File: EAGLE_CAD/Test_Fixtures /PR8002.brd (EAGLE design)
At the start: 118.5 x 99.3 mm, 61 parts, among them J1 M3_SCREW_POST

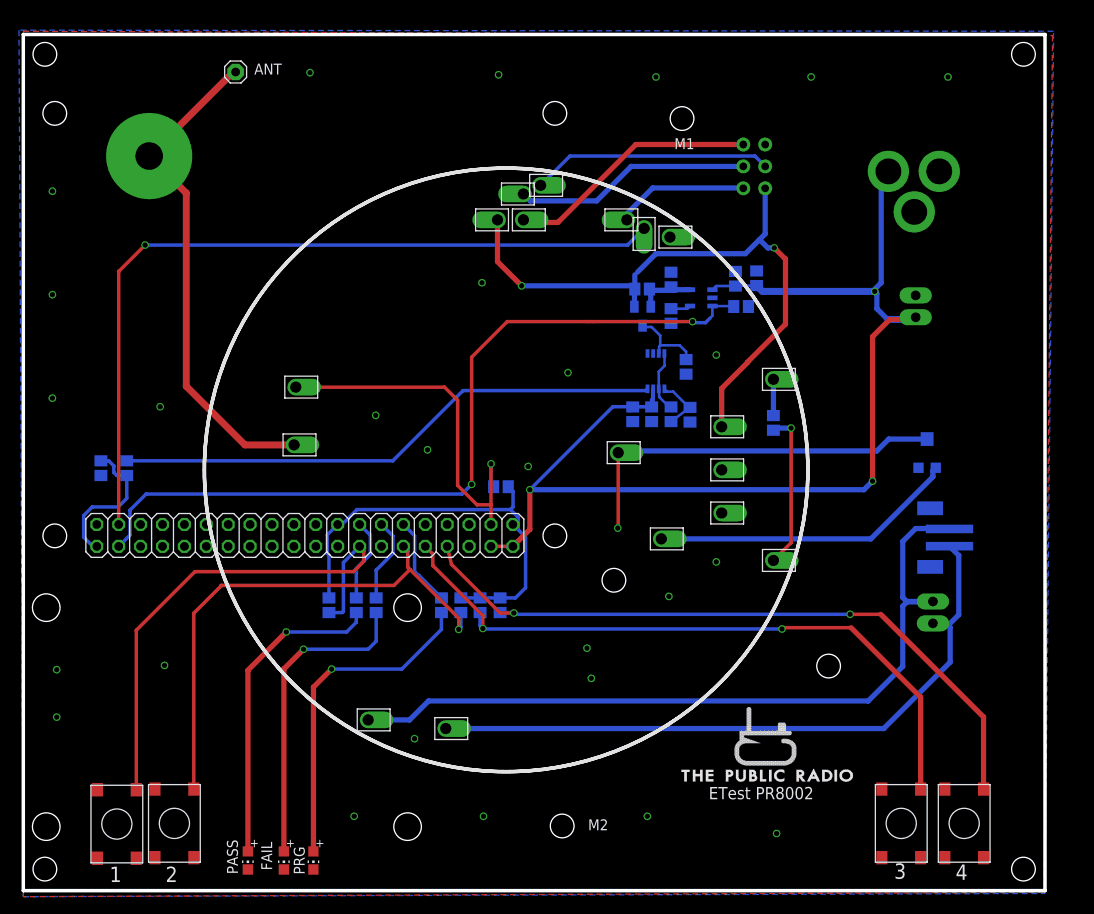
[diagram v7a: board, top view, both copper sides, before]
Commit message: edited test board outline
also aligned corner holes to a grid & moved ISP slightly
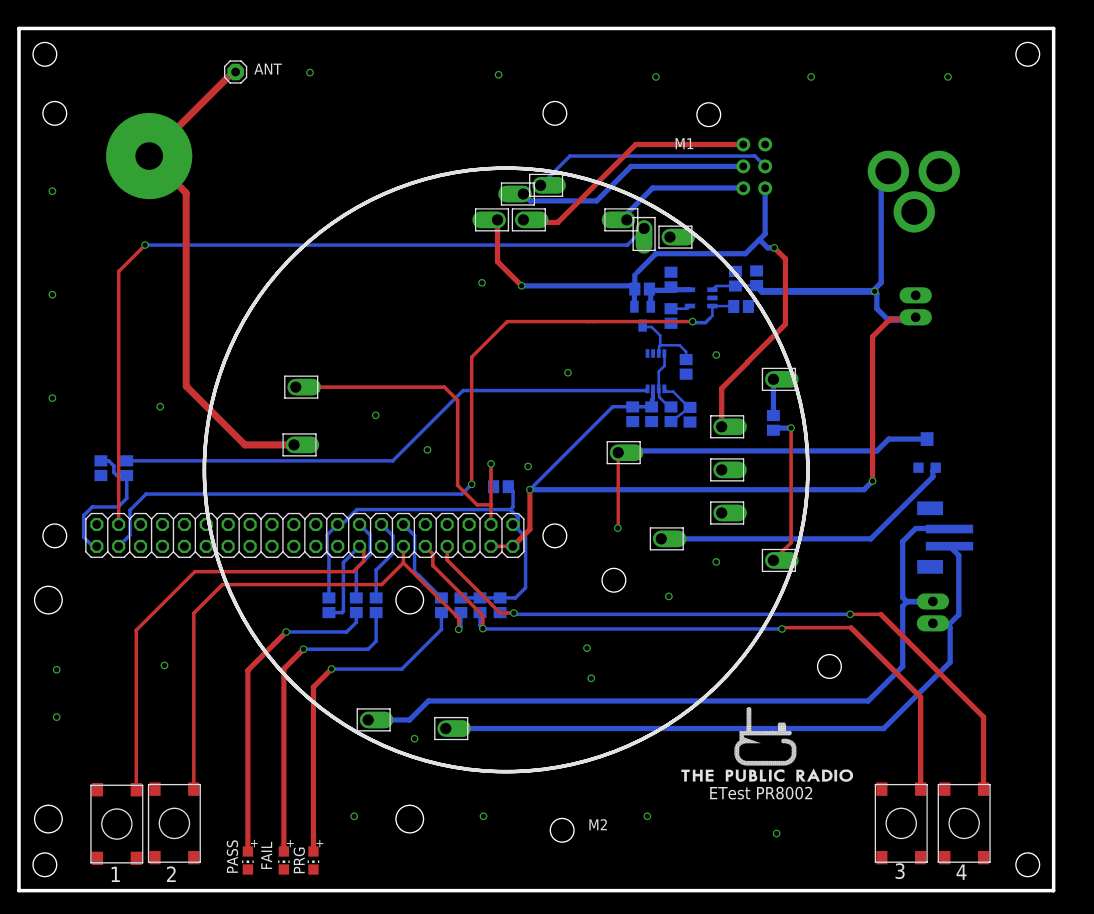
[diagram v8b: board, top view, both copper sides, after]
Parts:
- moved U$25 0.91 mm to (25.0, 21.0)
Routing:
- net TAC3: track 62.2 -> 61.6 mm
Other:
- board size 118.5 x 99.3 mm -> 120 x 100 mm
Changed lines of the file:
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@@
 <?xml version="1.0" encoding="utf-8"?>
 <!DOCTYPE eagle SYSTEM "eagle.dtd">
-<eagle version="6.6.0">
+<eagle version="7.2.0">
 <drawing>
 <settings>
@@
 <rectangle x1="56.8949" y1="26.4365" x2="56.9711" y2="26.4619" layer="26" rot="R180"/>
 <rectangle x1="56.9203" y1="26.4619" x2="57.0981" y2="26.4873" layer="26" rot="R180"/>
-<wire x1="0.5" y1="0" x2="119" y2="0" width="0.4064" layer="20"/>
-<wire x1="119" y1="0" x2="119" y2="99.3" width="0.4064" layer="20"/>
-<wire x1="119" y1="99.3" x2="0.5" y2="99.3" width="0.4064" layer="20"/>
-<wire x1="0.5" y1="99.3" x2="0.5" y2="0" width="0.4064" layer="20"/>
+<wire x1="0" y1="0" x2="120" y2="0" width="0.4064" layer="20"/>
+<wire x1="120" y1="0" x2="120" y2="100" width="0.4064" layer="20"/>
+<wire x1="120" y1="100" x2="0" y2="100" width="0.4064" layer="20"/>
+<wire x1="0" y1="100" x2="0" y2="0" width="0.4064" layer="20"/>
 <text x="80" y="10.6" size="1.4224" layer="25" font="vector" ratio="18">ETest PR8002</text>
 <wire x1="3.65" y1="93.65" x2="62.65" y2="93.65" width="0" layer="22"/>
@@
 <text x="22.675" y="68.225" size="1.778" layer="26" font="vector" ratio="16" rot="MR0">RPI B+</text>
 <circle x="56.5" y="48.8" radius="35" width="0.4064" layer="21"/>
-<hole x="63" y="7.5" drill="2.75"/>
-<hole x="76.9" y="89.55" drill="2.75"/>
+<hole x="63" y="7" drill="2.75"/>
+<hole x="80" y="90" drill="2.75"/>
 <text x="76" y="86" size="1.27" layer="21" font="vector" ratio="16">M1</text>
 <text x="66" y="7" size="1.27" layer="21" font="vector" ratio="16">M2</text>
-<hole x="3" y="2.5" drill="2.75"/>
+<hole x="3" y="3" drill="2.75"/>
 <hole x="3" y="97" drill="2.75"/>
-<hole x="116.5" y="97" drill="2.75"/>
+<hole x="117" y="97" drill="2.75"/>
 <hole x="69" y="36" drill="2.75"/>
-<hole x="116.5" y="2.5" drill="2.75"/>
-<hole x="93.9" y="26.05" drill="2.75"/>
+<hole x="117" y="3" drill="2.75"/>
+<hole x="94" y="26" drill="2.75"/>
 <text x="107.5" y="70.5" size="1.27" layer="22" font="vector" ratio="18" rot="MR270">+   -</text>
-<dimension x1="0.5" y1="-0.7" x2="37.75" y2="99.25" x3="126" y3="49.275" textsize="1.27" textratio="18" layer="20" dtype="vertical" unit="inch"/>
-<dimension x1="0.5" y1="99.675" x2="119" y2="99.3" x3="59.75" y3="102.5" textsize="1.27" textratio="18" layer="20" dtype="horizontal" unit="inch"/>
 </plain>
 <attributes>
@@
 <pass name="Default">
 <param name="RoutingGrid" value="50mil"/>
+<param name="AutoGrid" value="1"/>
+<param name="Efforts" value="0"/>
+<param name="TopRouterVariant" value="1"/>
 <param name="tpViaShape" value="round"/>
 <param name="PrefDir.1" value="|"/>
@@
 <attribute name="VALUE" x="23.855" y="91.775" size="1.27" layer="27"/>
 </element>
-<element name="U$25" library="PR_Parts_Library" package="SFUN_POCKETPROGRAMMER" value="SFUN_POCKETPROGRAMMER" x="24.75" y="20.125" rot="MR90"/>
+<element name="U$25" library="PR_Parts_Library" package="SFUN_POCKETPROGRAMMER" value="SFUN_POCKETPROGRAMMER" x="25" y="21" rot="MR90"/>
 <element name="GPIO" library="pinhead" package="2X20" value="" x="33.155" y="41.2" smashed="yes" rot="R180">
 <attribute name="NAME" x="27.555" y="46.025" size="1.27" layer="26" font="vector" ratio="16" rot="MR180"/>
@@
 <contactref element="ISP1" pad="6"/>
 <polygon width="0.6096" layer="1">
-<vertex x="0.5" y="99.675"/>
-<vertex x="119.875" y="99.175"/>
-<vertex x="118.875" y="-0.2"/>
-<vertex x="0.5" y="-0.7"/>
+<vertex x="0" y="100"/>
+<vertex x="120" y="100"/>
+<vertex x="120" y="0"/>
+<vertex x="0" y="0"/>
 </polygon>
 <polygon width="0.4064" layer="16">
-<vertex x="0.5" y="-0.7"/>
-<vertex x="119" y="-0.325"/>
-<vertex x="120" y="99.675"/>
-<vertex x="0" y="99.8"/>
+<vertex x="0" y="0"/>
+<vertex x="120" y="0"/>
+<vertex x="120" y="100"/>
+<vertex x="0" y="100"/>
 </polygon>
 <contactref element="U$3" pad="P$1"/>
@@
 <contactref element="GPIO" pad="8"/>
 <contactref element="R10" pad="2"/>
-<wire x1="49.665" y1="39.93" x2="50.165" y2="37.835" width="0.4064" layer="1"/>
 <via x="57.4" y="32.2" extent="1-16" drill="0.6" diameter="0.6096"/>
 <wire x1="57.4" y1="32.2" x2="57.35" y2="32.25" width="0.4064" layer="16"/>
@@
 <wire x1="96.4" y1="32.05" x2="99.95" y2="32.05" width="0.4064" layer="1"/>
 <wire x1="57.35" y1="32.25" x2="55.8" y2="32.25" width="0.4064" layer="16"/>
-<wire x1="50.165" y1="37.835" x2="55.8" y2="32.2" width="0.4064" layer="1"/>
 <wire x1="55.8" y1="32.2" x2="57.4" y2="32.2" width="0.4064" layer="1"/>
 <wire x1="99.95" y1="32.05" x2="111.875" y2="20.125" width="0.6096" layer="1"/>
 <wire x1="111.875" y1="20.125" x2="111.875" y2="11.775" width="0.6096" layer="1"/>
+<wire x1="55.8" y1="32.2" x2="49.665" y2="38.335" width="0.4064" layer="1"/>
+<wire x1="49.665" y1="38.335" x2="49.665" y2="39.93" width="0.4064" layer="1"/>
 </signal>
 <signal name="TAC2">
@@
 <contactref element="GPIO" pad="12"/>
 <contactref element="R12" pad="2"/>
-<wire x1="44.585" y1="39.93" x2="45.1" y2="39.415" width="0.4064" layer="1"/>
-<wire x1="45.1" y1="39.415" x2="45.1" y2="37.5" width="0.4064" layer="1"/>
-<wire x1="45.1" y1="37.5" x2="45.35" y2="37.25" width="0.4064" layer="1"/>
-<wire x1="45.35" y1="37.25" x2="51" y2="31.6" width="0.4064" layer="1"/>
 <wire x1="51" y1="31.6" x2="51" y2="30.3" width="0.4064" layer="1"/>
 <via x="51" y="30.3" extent="1-16" drill="0.6" diameter="0.6096"/>
 <wire x1="51" y1="30.3" x2="50.9" y2="30.2" width="0.4064" layer="16"/>
-<wire x1="23.4" y1="35.4" x2="23.5" y2="35.4" width="0.4064" layer="1"/>
-<wire x1="23.5" y1="35.4" x2="43.5" y2="35.4" width="0.4064" layer="1"/>
-<wire x1="43.5" y1="35.4" x2="45.35" y2="37.25" width="0.4064" layer="1"/>
 <wire x1="51.25" y1="32.25" x2="51.25" y2="30.55" width="0.4064" layer="16"/>
 <wire x1="51.25" y1="30.55" x2="51" y2="30.3" width="0.4064" layer="16"/>
 <wire x1="20.275" y1="11.775" x2="20.275" y2="32.175" width="0.4064" layer="1"/>
-<wire x1="20.275" y1="32.175" x2="23.5" y2="35.4" width="0.4064" layer="1"/>
+<wire x1="51" y1="31.6" x2="44.585" y2="38.015" width="0.4064" layer="1"/>
+<wire x1="44.585" y1="38.015" x2="44.585" y2="39.93" width="0.4064" layer="1"/>
+<wire x1="20.275" y1="32.175" x2="23.6" y2="35.5" width="0.4064" layer="1"/>
+<wire x1="23.6" y1="35.5" x2="42.07" y2="35.5" width="0.4064" layer="1"/>
+<wire x1="42.07" y1="35.5" x2="44.585" y2="38.015" width="0.4064" layer="1"/>
 </signal>
 <signal name="REG_ENABLE">
